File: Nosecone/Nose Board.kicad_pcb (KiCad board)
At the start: 2 copper layers, 12 parts, among them J1 Conn_01x02, J2 Conn_01x06, J3 Conn_02x03_Counter_Clockwise, U1 RS485_converter_ISL83488, U2 ATXMEGA16A4U-AU, U3 3.3V_DCDC_Conv_TPS62056DGS, U4 GPS_UBX_CAM_M8C, U5 GPS_UBX_CAM_M8C, U6 XBEE, U7 OpenLog

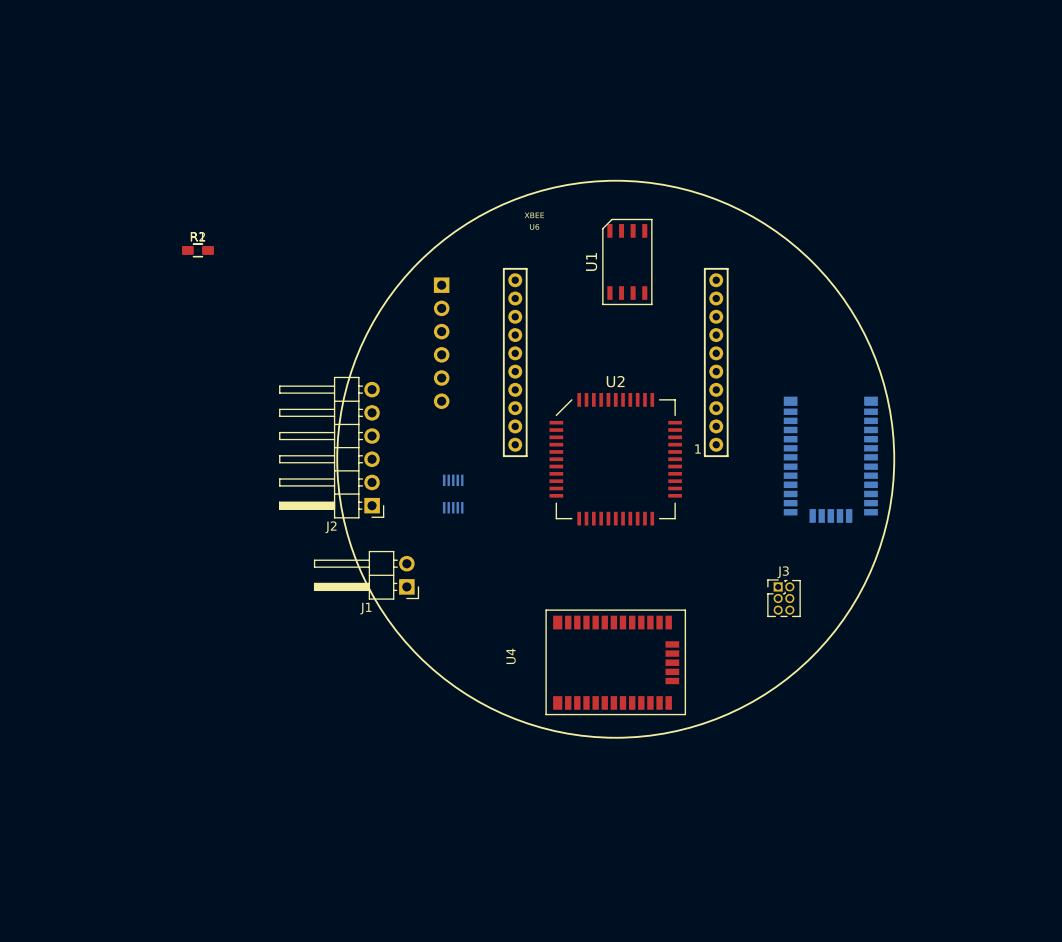
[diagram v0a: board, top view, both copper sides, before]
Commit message: Added pressure sensors, began routing
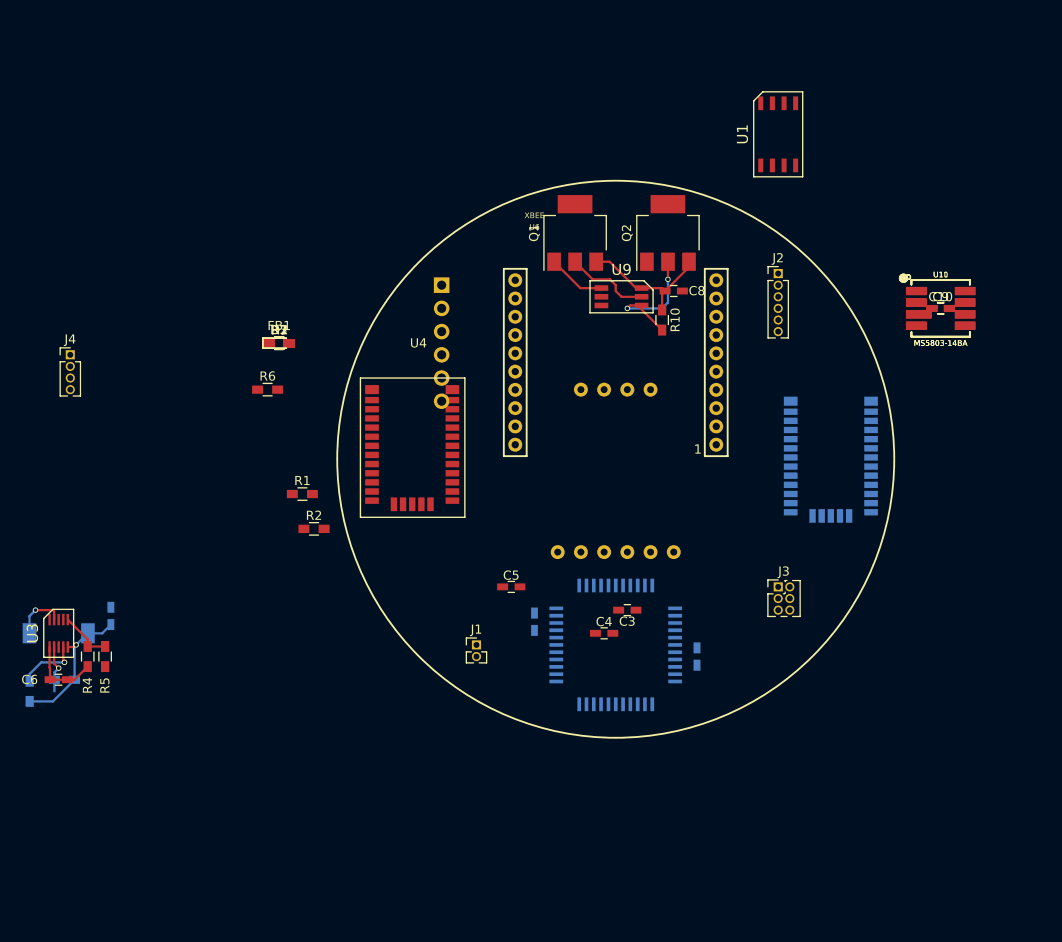
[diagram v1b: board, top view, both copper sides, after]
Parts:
- added C1: C, Capacitors_SMD:C_0603_HandSoldering, B.Cu at (151.1, 109.2)
- added C10, C9: 100nF, Capacitors_SMD:C_0603_HandSoldering, F.Cu at (195.6, 74.9)
- added C2: C, Capacitors_SMD:C_0603_HandSoldering, B.Cu at (168.9, 113.0)
- added C3: C, Capacitors_SMD:C_0603_HandSoldering, F.Cu at (161.3, 108.0)
- added C4: 10uF, Capacitors_SMD:C_0603_HandSoldering, F.Cu at (158.8, 110.5)
- added C5: 100nF, Capacitors_SMD:C_0603_HandSoldering, F.Cu at (148.6, 105.4)
- added C6: 10uF, Capacitors_SMD:C_0603_HandSoldering, F.Cu at (99.1, 115.6)
- added C7: 22uF, Capacitors_SMD:C_0603_HandSoldering, B.Cu at (104.8, 108.6)
- added C8: C, Capacitors_SMD:C_0603_HandSoldering, F.Cu at (166.4, 73.0)
- added D1, D2: LED, LEDs:LED_0603_HandSoldering, F.Cu at (123.2, 78.7)
- added FB1: FERRITE_BEAD-0603, Inductors_SMD:L_0603_HandSoldering, F.Cu at (123.2, 78.7)
- added J4: Conn_01x04, Pin_Headers:Pin_Header_Straight_1x04_Pitch1.27mm, F.Cu at (100.3, 80.0)
- added L1: 10uH, Inductors_SMD:L_7.3x7.3_H4.5, B.Cu at (99.1, 110.5)
- added Q1: Q_PMOS_DGS, TO_SOT_Packages_SMD:SOT-223-3_TabPin2, F.Cu at (155.6, 66.7)
- added Q2: Q_PMOS_DGS, TO_SOT_Packages_SMD:SOT-223-3_TabPin2, F.Cu at (165.7, 66.7)
- added R10: 470k, Resistors_SMD:R_0603_HandSoldering, F.Cu at (165.1, 76.2)
- added R3: 10k, Resistors_SMD:R_0603_HandSoldering, F.Cu at (123.2, 78.7)
- added R4: 130k, Resistors_SMD:R_0603_HandSoldering, F.Cu at (102.2, 113.0)
- added R5: 100k, Resistors_SMD:R_0603_HandSoldering, F.Cu at (104.1, 113.0)
- added R6: R, Resistors_SMD:R_0603_HandSoldering, F.Cu at (121.9, 83.8)
- added R7: R, Resistors_SMD:R_0603_HandSoldering, F.Cu at (123.2, 78.7)
- added R8: 1M, Resistors_SMD:R_0603_HandSoldering, B.Cu at (95.9, 116.8)
- added R9: 1M, Resistors_SMD:R_0603_HandSoldering, B.Cu at (99.7, 115.6)
- added U10, U11: MS5803-14BA, Silicon-Standard:MS5803, F.Cu at (195.6, 74.9)
- added U8: BNO055, Misc components:BNO055_Breakout, B.Cu at (166.4, 101.6)
- added U9: LTC4412, Misc components:SOIC-6, F.Cu at (160.7, 73.7)
- J1: footprint Pin_Headers:Pin_Header_Angled_1x02_Pitch2.54mm -> Pin_Headers:Pin_Header_Straight_1x02_Pitch1.27mm
- J2: footprint Pin_Headers:Pin_Header_Angled_1x06_Pitch2.54mm -> Pin_Headers:Pin_Header_Straight_1x06_Pitch1.27mm
- J3: value Conn_02x03_Counter_Clockwise -> Conn_02x03_Odd_Even
- U2: moved to B.Cu
- U3: moved to F.Cu
- moved J2 51.2 mm to (177.8, 71.1), turned to 0 degrees
- moved U3 45.8 mm to (99.1, 110.5)
- moved U4 39.9 mm to (133.3, 83.8), turned to 0 degrees
- moved R2 33.0 mm to (127.0, 99.1)
- moved R1 29.0 mm to (125.7, 95.2)
- moved U1 21.6 mm to (177.8, 55.9)
- moved U2 20.3 mm to (160.0, 111.8)
- moved J1 9.92 mm to (144.8, 111.8), turned to 0 degrees
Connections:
- J2 pad 1: (no net) -> VBUS
- J3 pad 1: (no net) -> /PDI_Data
- J3 pad 2: (no net) -> +3V3
- J3 pad 5: (no net) -> /PDI_CLK
- J3 pad 6: (no net) -> GND
- U1 pad 2: (no net) -> /Center_Dout
- U1 pad 3: (no net) -> /Center_Din
- U2 pad 10: (no net) -> /IMU_SDA
- U2 pad 11: (no net) -> /IMU_SCL
- U2 pad 12: (no net) -> /XBEE_Dout
- U2 pad 13: (no net) -> /XBEE_Din
- U2 pad 14: (no net) -> /P1_CS
- U2 pad 15: (no net) -> /P_MOSI
- U2 pad 16: (no net) -> /P_MISO
- U2 pad 17: (no net) -> /P_SCLK
- U2 pad 18: (no net) -> GND
- U2 pad 19: (no net) -> +3V3
- U2 pad 2: (no net) -> /P2_CS
- U2 pad 20: (no net) -> /GPS1_EXTINT
- U2 pad 21: (no net) -> /GPS2_EXTINT
- U2 pad 22: (no net) -> /GPS1_TXD
- U2 pad 23: (no net) -> /GPS1_RXD
- U2 pad 24: (no net) -> /LED_STATUS1
- U2 pad 25: (no net) -> /LED_STATUS2
- U2 pad 26: (no net) -> /GPS2_TXD
- U2 pad 27: (no net) -> /GPS2_RXD
- U2 pad 28: (no net) -> /GPS1_PPS
- U2 pad 29: (no net) -> /GPS2_PPS
- U2 pad 3: (no net) -> /IMU_INT
- U2 pad 30: (no net) -> GND
- U2 pad 31: (no net) -> +3V3
- U2 pad 32: (no net) -> /Center_Dout
- U2 pad 33: (no net) -> /Center_Din
- U2 pad 34: (no net) -> /PDI_Data
- U2 pad 35: (no net) -> /PDI_CLK
- U2 pad 38: (no net) -> GND
- U2 pad 39: (no net) -> Net-(C4-Pad2)
- U2 pad 8: (no net) -> GND
- U2 pad 9: (no net) -> +3V3
- U3 pad 1: (no net) -> VDC
- U3 pad 10: (no net) -> GND
- U3 pad 2: (no net) -> Net-(R9-Pad2)
- U3 pad 3: (no net) -> GND
- U3 pad 4: (no net) -> Net-(R8-Pad2)
- U3 pad 5: (no net) -> +3V3
- U3 pad 6: (no net) -> Net-(R4-Pad2)
- U3 pad 7: (no net) -> GND
- U3 pad 8: (no net) -> VDC
- U3 pad 9: (no net) -> Net-(L1-Pad2)
- U4 pad 25: (no net) -> /GPS1_TXD
- U4 pad 26: (no net) -> /GPS1_RXD
- U4 pad 29: (no net) -> /GPS1_PPS
- U4 pad 7: (no net) -> /GPS1_EXTINT
- U5 pad 25: (no net) -> /GPS2_TXD
- U5 pad 26: (no net) -> /GPS2_RXD
- U5 pad 29: (no net) -> /GPS2_PPS
- U5 pad 7: (no net) -> /GPS2_EXTINT
- U6 pad 1: (no net) -> +3V3
- U6 pad 10: (no net) -> GND
- U6 pad 2: (no net) -> /XBEE_Dout
- U6 pad 3: (no net) -> /XBEE_Din
- U7 pad 2: (no net) -> /XBEE_Din
- U7 pad 4: (no net) -> +3V3
- U7 pad 5: (no net) -> GND
- U7 pad 6: (no net) -> GND
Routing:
- net VDC: track 0.00 -> 23.5 mm
- net +3V3: track 0.00 -> 15.5 mm, vias 0 -> 1
- net Net-(Q2-Pad2): track 0.00 -> 14.5 mm, vias 0 -> 2
- net Net-(Q1-Pad2): track 0.00 -> 9.24 mm
- net Net-(R8-Pad2): track 0.00 -> 6.87 mm, vias 0 -> 1
- net +BATT: track 0.00 -> 6.38 mm
- net Net-(L1-Pad2): track 0.00 -> 5.81 mm, vias 0 -> 1
- net Net-(R4-Pad2): track 0.00 -> 5.75 mm
- net Net-(R9-Pad2): track 0.00 -> 5.25 mm, vias 0 -> 1

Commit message: Continued routing
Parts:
- C10, C6, C9, R4, R5, U3: moved to B.Cu
- C7, L1, R8, R9: moved to F.Cu
- moved U7 65.0 mm to (206.0, 73.4), turned to 0 degrees
- moved L1 64.6 mm to (161.6, 94.3), turned to 270 degrees
- moved U3 64.6 mm to (161.6, 94.3), turned to 90 degrees
- moved R8 62.5 mm to (155.3, 97.5), turned to 0 degrees
- moved C7 62.0 mm to (163.5, 88.6), turned to 0 degrees
- moved C6 61.3 mm to (156.5, 94.3), turned to 90 degrees
- moved R9 60.9 mm to (156.5, 93.7), turned to 270 degrees
- moved R4 60.9 mm to (159.1, 91.1), turned to 0 degrees
- moved R5 59.9 mm to (159.1, 89.2), turned to 180 degrees
- moved C9 44.9 mm to (175.0, 114.8)
- moved U10 43.8 mm to (174.0, 113.0)
- moved C10 36.2 mm to (180.8, 108.0), turned to 180 degrees
- moved U11 33.0 mm to (181.6, 104.8), turned to 270 degrees
- moved J3 29.6 mm to (182.9, 76.2)
- moved U2 3.18 mm to (156.8, 111.8), turned to 270 degrees
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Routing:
- net +3V3: track 15.5 -> 43.6 mm, vias 1 -> 4
- net /P_SCLK: track 0.00 -> 27.5 mm, vias 0 -> 1
- net /P_MOSI: track 0.00 -> 25.1 mm, vias 0 -> 3
- net /P_MISO: track 0.00 -> 23.6 mm, vias 0 -> 1
- net /P1_CS: track 0.00 -> 22.5 mm, vias 0 -> 1

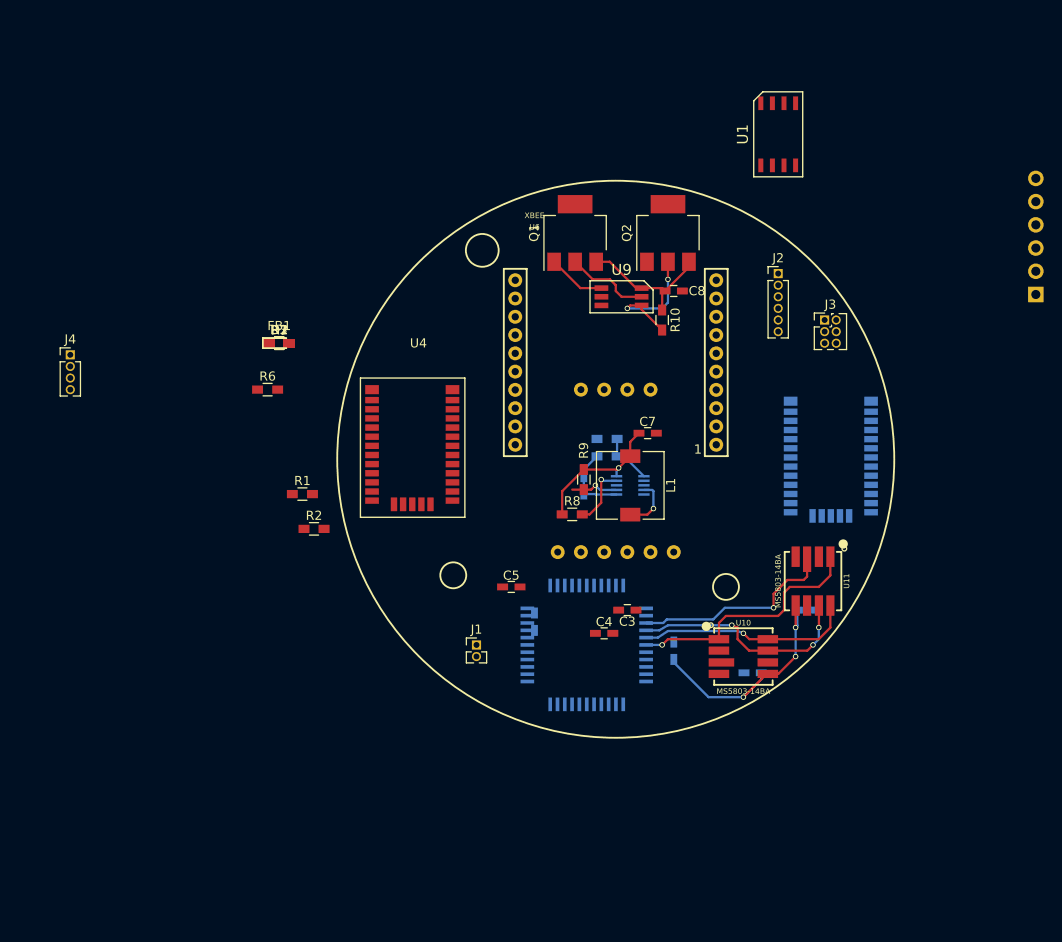
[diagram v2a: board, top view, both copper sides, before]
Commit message: Placement adjustments
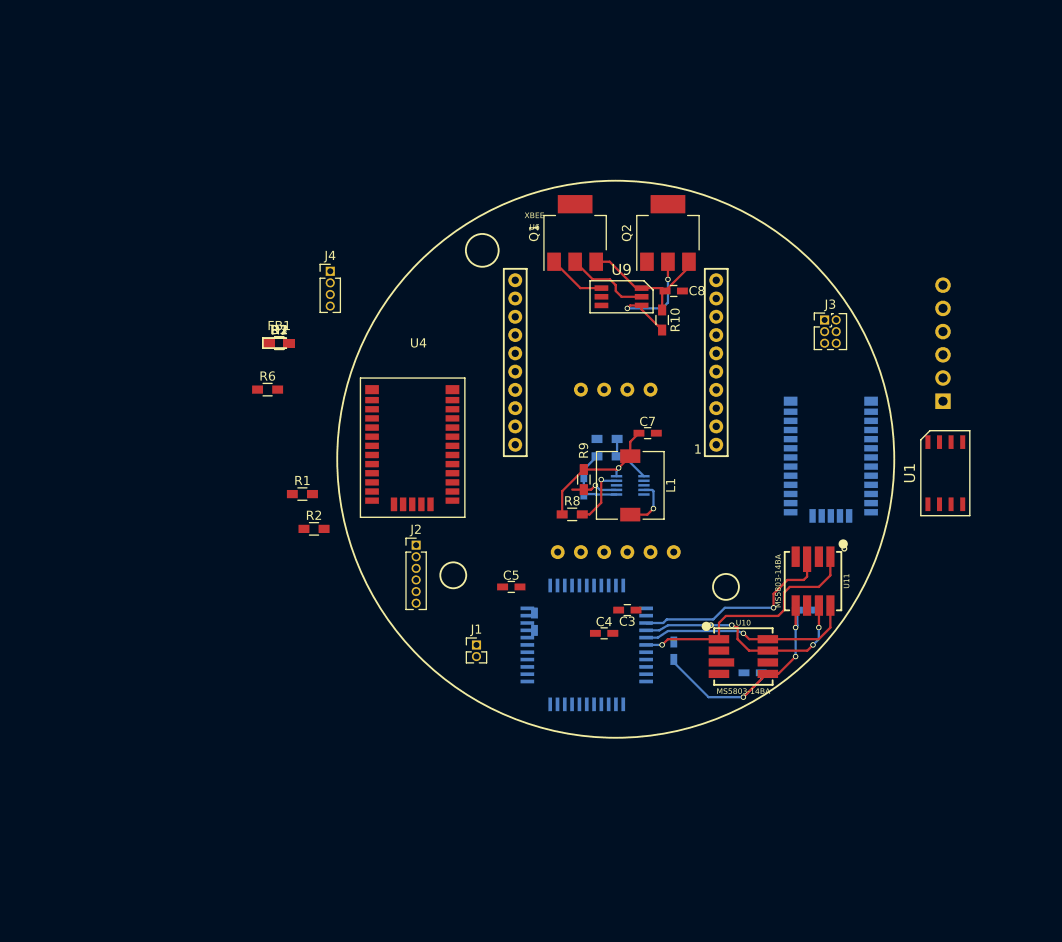
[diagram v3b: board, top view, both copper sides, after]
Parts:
- moved J2 49.5 mm to (138.2, 100.8)
- moved U1 41.3 mm to (196.1, 93.0)
- moved J4 29.9 mm to (128.8, 70.9)
- moved U7 15.5 mm to (195.8, 85.1)
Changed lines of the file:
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@@
   )
   (module "Misc components:SOIC-8" (layer F.Cu)
-    (at 177.8 55.88)
+    (at 196.088 92.964)
     (fp_text reference U1 (at -3.88 0 90) (layer F.SilkS)
       (effects (font (size 1.2 1.2) (thickness 0.15)))
@@
   )
   (module Pin_Headers:Pin_Header_Straight_1x06_Pitch2.54mm (layer B.Cu)
-    (at 205.994 73.406)
+    (at 195.834 85.09)
     (descr "Through hole straight pin header, 1x06, 2.54mm pitch, single row")
     (tags "Through hole pin header THT 1x06 2.54mm single row")
@@
   )
   (module Pin_Headers:Pin_Header_Straight_1x04_Pitch1.27mm (layer F.Cu)
-    (at 100.33 80.01)
+    (at 128.778 70.866)
     (descr "Through hole straight pin header, 1x04, 1.27mm pitch, single row")
     (tags "Through hole pin header THT 1x04 1.27mm single row")
@@
   )
   (module Pin_Headers:Pin_Header_Straight_1x06_Pitch1.27mm (layer F.Cu)
-    (at 177.8 71.12)
+    (at 138.176 100.838)
     (descr "Through hole straight pin header, 1x06, 1.27mm pitch, single row")
     (tags "Through hole pin header THT 1x06 1.27mm single row")

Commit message: PCB Routed
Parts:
- added C11: 4.7uF, Capacitors_SMD:C_0603_HandSoldering, B.Cu at (151.1, 69.2)
- added R11: 220, Resistors_SMD:R_0603_HandSoldering, B.Cu at (165.1, 72.4)
- added R12: 220, Resistors_SMD:R_0603_HandSoldering, B.Cu at (162.6, 74.9)
- added U12: Via-stitch, Misc components:Small-via, F.Cu at (163.9, 58.4)
- added U13: Via-stitch, Misc components:Small-via, F.Cu at (149.3, 58.6)
- C1, C10, C2, C9: moved to F.Cu
- C3, U1, U4: moved to B.Cu
- J2: value Conn_01x06 -> Conn_02x04_Odd_Even; footprint Pin_Headers:Pin_Header_Straight_1x06_Pitch1.27mm -> Connectors_JST:JST_PUD_B08B-PUDSS_2x04x2.00mm_Straight; moved to B.Cu
- J4: value Conn_01x04 -> Conn_Coaxial; footprint Pin_Headers:Pin_Header_Straight_1x04_Pitch1.27mm -> Connectors:SMA_THT_Jack_Straight
- U5: value GPS_UBX_CAM_M8C -> Via-stitch; footprint Misc components:UBX_CAM-M8C -> Misc components:Small-via; moved to F.Cu
- moved U1 61.1 mm to (142.2, 64.1), turned to 180 degrees
- moved R3 56.7 mm to (177.8, 94.0), turned to 180 degrees
- moved FB1 53.8 mm to (174.6, 94.6), turned to 90 degrees
- moved J4 47.5 mm to (175.3, 61.0)
- moved R7 45.9 mm to (165.7, 95.9), turned to 90 degrees
- moved D2 44.4 mm to (165.7, 91.4), turned to 90 degrees
- moved R6 43.0 mm to (163.2, 95.9), turned to 90 degrees
- moved D1 42.0 mm to (163.2, 91.4), turned to 90 degrees
- moved U4 38.7 mm to (162.6, 58.4), turned to 180 degrees
- moved U5 37.5 mm to (150.7, 89.5), turned to 0 degrees
- moved U11 36.8 mm to (147.3, 91.4), turned to 0 degrees
- moved C10 32.0 mm to (152.4, 93.3), turned to 270 degrees
- moved U10 30.1 mm to (147.3, 99.1)
- moved R1 29.6 mm to (152.4, 82.4), turned to 270 degrees
- moved U8 29.2 mm to (137.2, 101.6), turned to 0 degrees
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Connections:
- J4 pad 1: +3V3 -> Net-(J4-Pad1)
- U2 pad 21: /GPS2_EXTINT -> /IMU_INT
- U2 pad 26: /GPS2_TXD -> /Debug_RX
- U2 pad 27: /GPS2_RXD -> /Debug_TX
- U2 pad 29: /GPS2_PPS -> (no net)
- U2 pad 3: /IMU_INT -> (no net)
- U4 pad 16: Net-(U4-Pad16) -> (no net)
- U4 pad 17: Net-(U4-Pad16) -> Net-(J4-Pad1)
- U4 pad 25: /GPS1_TXD -> Net-(R11-Pad1)
- U4 pad 26: /GPS1_RXD -> Net-(R12-Pad1)
- U5 pad 1: +3V3 -> GND
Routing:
- net +3V3: track 43.6 -> 227.6 mm, vias 4 -> 6
- net /Center_Din: track 0.00 -> 61.6 mm, vias 0 -> 2
- net VDC: track 23.5 -> 83.6 mm, vias 0 -> 3
- net /Center_Dout: track 0.00 -> 58.8 mm, vias 0 -> 2
- net /Vbatt_meas: track 0.00 -> 47.9 mm, vias 0 -> 1
- net /Debug_RX: track 0.00 -> 45.0 mm, vias 0 -> 5
- net VBUS: track 0.00 -> 41.3 mm, vias 0 -> 2
- net /XBEE_Din: track 0.00 -> 41.1 mm, vias 0 -> 1
- net /Debug_TX: track 0.00 -> 38.2 mm, vias 0 -> 5
- net /P2_CS: track 0.00 -> 36.0 mm, vias 0 -> 1
- net /GPS1_EXTINT: track 0.00 -> 35.1 mm, vias 0 -> 2
- net /XBEE_Dout: track 0.00 -> 30.0 mm, vias 0 -> 1
- net /IMU_SDA: track 0.00 -> 29.6 mm
- net /IMU_SCL: track 0.00 -> 27.7 mm
- net +BATT: track 6.38 -> 31.9 mm, vias 0 -> 1
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- added copper zone on B.Cu, net GND
- added copper zone on F.Cu, net GND
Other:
- board outline added: 45.7 x 58.4 mm
- net class Default: clearance 0.2 -> 0.18
- rule trace_clearance: 0.2 -> 0.18
- rule trace_min: 0.2 -> 0.18

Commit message: Minor board adjustments, BoM work
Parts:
- added BZ1: Buzzer, Misc components:Buzzer-CUI_CEP-2242, F.Cu at (149.9, 111.8)
- added J5: Conn_01x02, Pin_Headers:Pin_Header_Straight_1x02_Pitch2.54mm, F.Cu at (162.1, 114.4)
- C1, C2, C3: value C -> 100nF
- C7: footprint Capacitors_SMD:C_0603_HandSoldering -> Capacitors_SMD:C_0805_HandSoldering
- J1: footprint Pin_Headers:Pin_Header_Straight_1x02_Pitch1.27mm -> Connectors_JST:JST_PH_B2B-PH-K_02x2.00mm_Straight
- moved C3 0.38 mm to (163.8, 102.5)
- moved C7 0.27 mm to (177.5, 102.0)
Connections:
- U2 pad 29: (no net) -> /Buzzer_drive
- U2 pad 41: (no net) -> /A1
- U2 pad 42: (no net) -> /A2
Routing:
- net /A2: track 0.00 -> 41.7 mm, vias 0 -> 1
- net GND: track 5.07 -> 46.0 mm, vias 0 -> 4
- net /Debug_RX: track 45.0 -> 4.05 mm, vias 5 -> 1
- net /A1: track 0.00 -> 38.5 mm
- net /Buzzer_drive: track 0.00 -> 30.2 mm, vias 0 -> 4
- net /P2_CS: track 36.0 -> 35.5 mm
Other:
- board size 45.7 x 58.4 mm -> 45.7 x 63.5 mm
